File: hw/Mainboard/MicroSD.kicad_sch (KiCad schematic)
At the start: 6 parts, among them J24 MicroSD

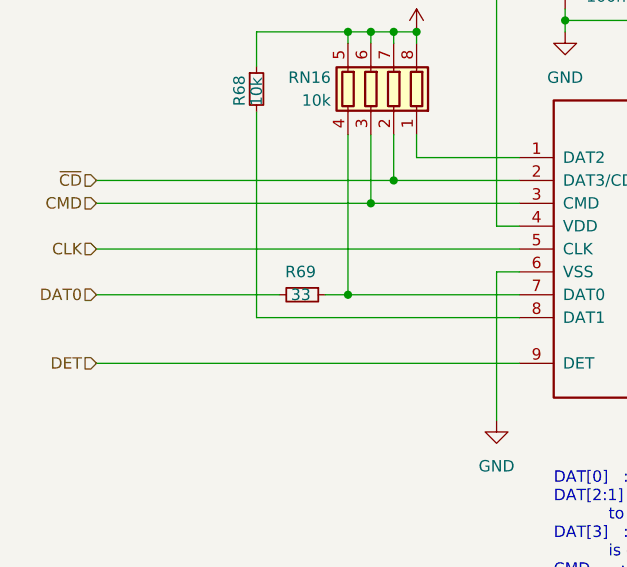
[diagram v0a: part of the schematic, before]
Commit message: hw: remove series termination, gnd under hdmi (wip)
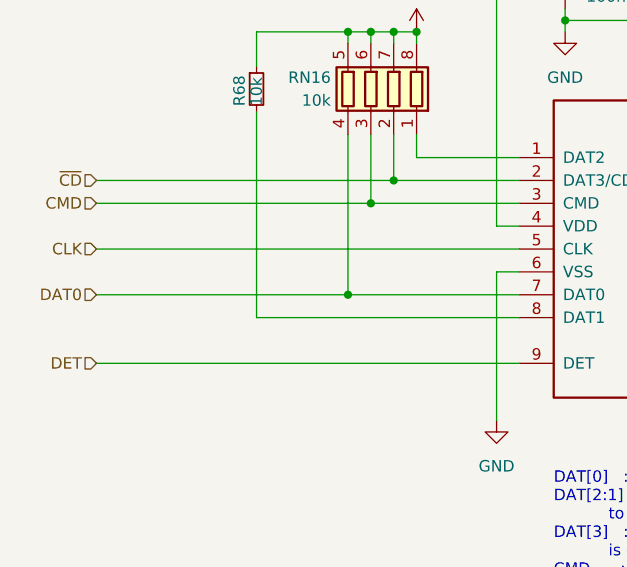
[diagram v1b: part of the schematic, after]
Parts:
- removed R69: 33, Resistor_SMD:R_0402_1005Metric, symbol Device:R_Small
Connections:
- net DAT0: now also J24.7 (DAT0), RN16.4 (R4.1)
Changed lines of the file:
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@@
-    (stroke (width 0) (type default) (color 0 0 0 0))
-  )
-  (wire (pts (xy 102.87 104.14) (xy 123.19 104.14))
     (stroke (width 0) (type default) (color 0 0 0 0))
   )
@@
     (stroke (width 0) (type default) (color 0 0 0 0))
   )
-  (wire (pts (xy 128.27 104.14) (xy 130.81 104.14))
+  (wire (pts (xy 102.87 104.14) (xy 130.81 104.14))
     (stroke (width 0) (type default) (color 0 0 0 0))
   )
@@
     (pin "1")
   )
-  (symbol (lib_id "Device:R_Small") (at 125.73 104.14 270) (unit 1)
-    (in_bom yes) (on_board yes)
-    (property "Reference" "R69" (id 0) (at 123.825 101.6 90)
-      (effects (font (size 1.27 1.27)) (justify left))
-    )
-    (property "Value" "33" (id 1) (at 124.46 104.14 90)
-      (effects (font (size 1.27 1.27)) (justify left))
-    )
-    (property "Footprint" "Resistor_SMD:R_0402_1005Metric" (id 2) (at 125.73 104.14 0)
-      (effects (font (size 1.27 1.27)) hide)
-    )
-    (property "Datasheet" "https://datasheet.lcsc.com/lcsc/2205311900_UNI-ROYAL-Uniroyal-Elec-0402WGF330JTCE_C25105.pdf" (id 3) (at 125.73 104.14 0)
-      (effects (font (size 1.27 1.27)) hide)
-    )
-    (property "LCSC" "C25105" (id 4) (at 125.73 104.14 0)
-      (effects (font (size 1.27 1.27)) hide)
-    )
-    (pin "1")
-    (pin "2")
-  )
   (symbol (lib_id "Device:C_Small") (at 154.94 69.85 0) (unit 1)

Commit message: hw: caps & logos (wip)
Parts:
- C83: value 10u 6.3V -> 47u 10V; footprint Capacitor_SMD:C_0402_1005Metric -> Capacitor_SMD:C_1206_3216Metric; LCSC C15525 -> C96123
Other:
- note added: "47uF decoupling capacitor handles inrush current from hot insertion."
- title: CBM PET Mainboard Replacement -> EconoPET 40/8096
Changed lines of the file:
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@@
   (paper "A")
   (title_block
-    (title "CBM PET Mainboard Replacement")
+    (title "EconoPET 40/8096")
+    (date "2023-10-01")
+    (rev "A")
   )
   (junction (at 130.81 104.14) (diameter 0) (color 0 0 0 0)
@@
   (wire (pts (xy 133.35 74.93) (xy 133.35 76.2))
     (stroke (width 0) (type default) (color 0 0 0 0))
+  )
+  (text "47uF decoupling capacitor handles\ninrush current from hot insertion."
+    (at 180.34 71.12 0)
+    (effects (font (size 1.27 1.27)) (justify left bottom))
   )
   (text "DAT[0]   : (POCI) is open-drain output that requires pullup.\nDAT[2:1] : Unused inputs in SPI mode.  Pullups recommended\n           to avoid current draw due to metastablitiy.\nDAT[3]   : (~{CS}) has built-in 22-50k pullup to ensure card\n           is deselected by default.\nCMD      : (PICO) input in SPI mode.\nCLK      : (SCK) always an input.  Never gets pullup.\n\nCM1624 uses:\n25k pullup for DAT[0:3] and CMD\n40 Ohm termination for DAT[0:3], CMD, and CLK\n\n10k pullups common (e.g., ExpressIf documentation)."
@@
     (pin "1")
   )
-  (symbol (lib_id "Device:C_Small") (at 165.1 69.85 0) (unit 1)
-    (in_bom yes) (on_board yes)
-    (property "Reference" "C83" (id 0) (at 167.4368 68.6816 0)
-      (effects (font (size 1.27 1.27)) (justify left))
-    )
-    (property "Value" "10u 6.3V" (id 1) (at 167.4368 70.993 0)
-      (effects (font (size 1.27 1.27)) (justify left))
-    )
-    (property "Footprint" "Capacitor_SMD:C_0402_1005Metric" (id 2) (at 165.1 69.85 0)
-      (effects (font (size 1.27 1.27)) hide)
-    )
-    (property "Datasheet" "https://datasheet.lcsc.com/lcsc/2208231630_Samsung-Electro-Mechanics-CL05A106MQ5NUNC_C15525.pdf" (id 3) (at 165.1 69.85 0)
-      (effects (font (size 1.27 1.27)) hide)
-    )
-    (property "LCSC" "C15525" (id 4) (at 165.1 69.85 0)
-      (effects (font (size 1.27 1.27)) hide)
-    )
-    (pin "1")
-    (pin "2")
-  )
   (symbol (lib_id "Device:R_Small") (at 120.65 81.28 0) (unit 1)
     (in_bom yes) (on_board yes)
@@
     (pin "1")
   )
+  (symbol (lib_id "Device:C_Small") (at 165.1 69.85 0) (unit 1)
+    (in_bom yes) (on_board yes)
+    (property "Reference" "C83" (id 0) (at 167.4368 68.6816 0)
+      (effects (font (size 1.27 1.27)) (justify left))
+    )
+    (property "Value" "47u 10V" (id 1) (at 167.4368 70.993 0)
+      (effects (font (size 1.27 1.27)) (justify left))
+    )
+    (property "Footprint" "Capacitor_SMD:C_1206_3216Metric" (id 2) (at 165.1 69.85 0)
+      (effects (font (size 1.27 1.27)) hide)
+    )
+    (property "Datasheet" "https://datasheet.lcsc.com/lcsc/1810221121_Samsung-Electro-Mechanics-CL31A476MPHNNNE_C96123.pdf" (id 3) (at 165.1 69.85 0)
+      (effects (font (size 1.27 1.27)) hide)
+    )
+    (property "LCSC" "C96123" (id 4) (at 165.1 69.85 0)
+      (effects (font (size 1.27 1.27)) hide)
+    )
+    (pin "1")
+    (pin "2")
+  )
   (symbol (lib_id "Device:C_Small") (at 154.94 69.85 0) (unit 1)

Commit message: hw: renumber J* refs to match PET connectors
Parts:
- J23: renamed from J24; value MicroSD -> MICRO_SD
- renumbered C82 to C98, C83 to C99, R68 to R55
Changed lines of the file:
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@@
   (symbol (lib_id "power:+3V3") (at 138.43 74.93 0) (mirror y) (unit 1)
     (in_bom yes) (on_board yes)
-    (property "Reference" "#PWR0153" (id 0) (at 138.43 78.74 0)
+    (property "Reference" "#PWR0165" (id 0) (at 138.43 78.74 0)
       (effects (font (size 1.27 1.27)) hide)
     )
@@
   (symbol (lib_id "power:+3V3") (at 147.32 64.77 0) (unit 1)
     (in_bom yes) (on_board yes)
-    (property "Reference" "#PWR0152" (id 0) (at 147.32 68.58 0)
+    (property "Reference" "#PWR0166" (id 0) (at 147.32 68.58 0)
       (effects (font (size 1.27 1.27)) hide)
     )
@@
   (symbol (lib_id "Connector:Micro_SD_Card_Det") (at 172.72 99.06 0) (unit 1)
     (in_bom yes) (on_board yes) (fields_autoplaced)
-    (property "Reference" "J24" (id 0) (at 173.355 77.47 0))
-    (property "Value" "MicroSD" (id 1) (at 173.355 80.01 0))
+    (property "Reference" "J23" (id 0) (at 173.355 77.47 0))
+    (property "Value" "MICRO_SD" (id 1) (at 173.355 80.01 0))
     (property "Footprint" "JLCPCB:TF-SMD_TF-PUSH" (id 2) (at 224.79 81.28 0)
       (effects (font (size 1.27 1.27)) hide)
@@
   (symbol (lib_id "power:GND") (at 194.31 113.03 0) (unit 1)
     (in_bom yes) (on_board yes) (fields_autoplaced)
-    (property "Reference" "#PWR0155" (id 0) (at 194.31 119.38 0)
+    (property "Reference" "#PWR0169" (id 0) (at 194.31 119.38 0)
       (effects (font (size 1.27 1.27)) hide)
     )
@@
   (symbol (lib_id "power:GND") (at 147.32 118.11 0) (unit 1)
     (in_bom yes) (on_board yes) (fields_autoplaced)
-    (property "Reference" "#PWR0156" (id 0) (at 147.32 124.46 0)
+    (property "Reference" "#PWR0167" (id 0) (at 147.32 124.46 0)
       (effects (font (size 1.27 1.27)) hide)
     )
@@
   (symbol (lib_id "Device:R_Small") (at 120.65 81.28 0) (unit 1)
     (in_bom yes) (on_board yes)
-    (property "Reference" "R68" (id 0) (at 118.745 83.185 90)
+    (property "Reference" "R55" (id 0) (at 118.745 83.185 90)
       (effects (font (size 1.27 1.27)) (justify left))
     )
@@
   (symbol (lib_id "power:GND") (at 154.94 74.93 0) (unit 1)
     (in_bom yes) (on_board yes) (fields_autoplaced)
-    (property "Reference" "#PWR0154" (id 0) (at 154.94 81.28 0)
+    (property "Reference" "#PWR0168" (id 0) (at 154.94 81.28 0)
       (effects (font (size 1.27 1.27)) hide)
     )
@@
   (symbol (lib_id "Device:C_Small") (at 165.1 69.85 0) (unit 1)
     (in_bom yes) (on_board yes)
-    (property "Reference" "C83" (id 0) (at 167.4368 68.6816 0)
+    (property "Reference" "C99" (id 0) (at 167.4368 68.6816 0)
       (effects (font (size 1.27 1.27)) (justify left))
     )
@@
   (symbol (lib_id "Device:C_Small") (at 154.94 69.85 0) (unit 1)
     (in_bom yes) (on_board yes)
-    (property "Reference" "C82" (id 0) (at 157.2768 68.6816 0)
+    (property "Reference" "C98" (id 0) (at 157.2768 68.6816 0)
       (effects (font (size 1.27 1.27)) (justify left))
     )
